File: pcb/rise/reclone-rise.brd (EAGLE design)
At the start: 85 x 56 mm, 11 parts, among them J1 MAGJACK, U1 6SLX25FTG256

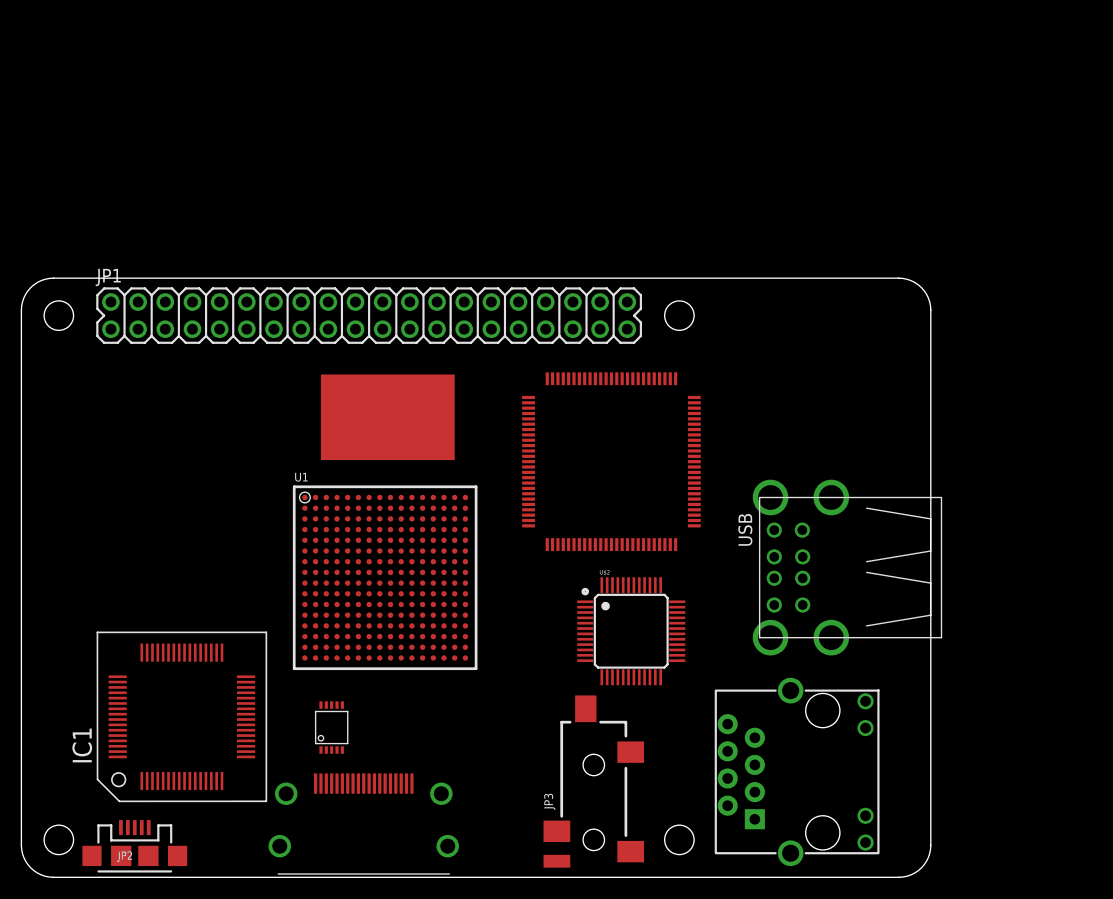
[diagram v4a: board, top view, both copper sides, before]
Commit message: Added Gadgeteer socket
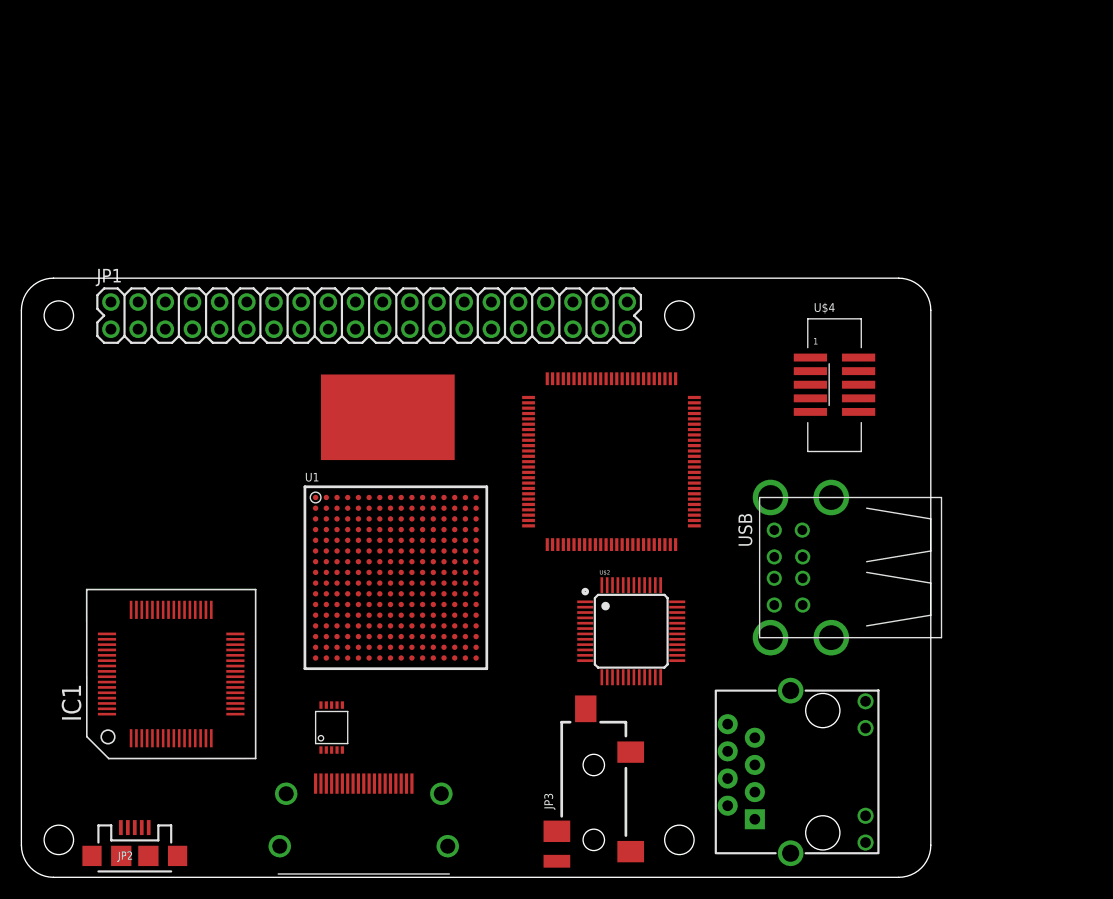
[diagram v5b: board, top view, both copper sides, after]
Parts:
- added U$4: SHF105, Gadgeteer:SHF105DSM_1
- U1: value 6SLX25FTG256 -> 6SLX16FTG256
- moved IC1 4.12 mm to (14.0, 19.0)
- moved U1 1.00 mm to (35.0, 28.0)
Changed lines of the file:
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@@
 <element name="USB" library="reclone-rise" package="USB-A-2H" value="USB_A_2H" x="69" y="29" locked="yes" rot="R180"/>
 <element name="MCU" library="reclone-rise" package="LQFP-100" value="STM32F407VGT6" x="48" y="46" rot="R270"/>
-<element name="U1" library="xilinx_devices_V6" package="FT256" value="6SLX25FTG256" x="34" y="28"/>
 <element name="JP1" library="SparkFun-Connectors" package="2X20" value="M20X2" x="32.5" y="52.5" locked="yes"/>
 <element name="J1" library="SparkFun-Connectors" package="MAGJACK" value="MAGJACK" x="86" y="2.25" locked="yes" rot="R90"/>
-<element name="IC1" library="ftdichip-3" package="TQFP64-12X12" value="" x="15" y="15"/>
+<element name="IC1" library="ftdichip-3" package="TQFP64-12X12" value="" x="14" y="19"/>
 <element name="JP2" library="SparkFun-Connectors" package="USB-MICROB" value="USB-MICROB" x="10.6" y="2" locked="yes">
 <attribute name="PROD_ID" value="CONN-09505" x="10.6" y="2" size="1.778" layer="27" display="off"/>
@@
 <element name="U$2" library="reclone-rise" package="LQFP-48" value="DP83848C" x="57" y="23"/>
 <element name="U$3" library="reclone-rise" package="HDMI_A_SMT" value="HDMI_A" x="32" y="4" locked="yes" rot="R270"/>
+<element name="U1" library="xilinx_devices_V6" package="FT256" value="6SLX16FTG256" x="35" y="28"/>
+<element name="U$4" library="Gadgeteer" package="SHF105DSM_1" value="SHF105" x="76" y="46"/>
 </elements>
 <signals>
 <signal name="GND">
+<contactref element="IC1" pad="1"/>
+<contactref element="IC1" pad="5"/>
+<contactref element="IC1" pad="11"/>
+<contactref element="IC1" pad="15"/>
+<contactref element="IC1" pad="25"/>
+<contactref element="IC1" pad="35"/>
+<contactref element="IC1" pad="47"/>
+<contactref element="IC1" pad="51"/>
 <contactref element="U1" pad="A1"/>
 <contactref element="U1" pad="A16"/>
@@
 <contactref element="U1" pad="T1"/>
 <contactref element="U1" pad="T16"/>
-<contactref element="IC1" pad="1"/>
-<contactref element="IC1" pad="5"/>
-<contactref element="IC1" pad="11"/>
-<contactref element="IC1" pad="15"/>
-<contactref element="IC1" pad="25"/>
-<contactref element="IC1" pad="35"/>
-<contactref element="IC1" pad="47"/>
-<contactref element="IC1" pad="51"/>
-<wire x1="38.5" y1="32.5" x2="41.5" y2="35.5" width="0" layer="19" extent="1-1"/>
-<wire x1="36.5" y1="34.5" x2="38.5" y2="32.5" width="0" layer="19" extent="1-1"/>
-<wire x1="40.5" y1="29.5" x2="38.5" y2="32.5" width="0" layer="19" extent="1-1"/>
-<wire x1="37.5" y1="28.5" x2="40.5" y2="29.5" width="0" layer="19" extent="1-1"/>
-<wire x1="34.5" y1="28.5" x2="37.5" y2="28.5" width="0" layer="19" extent="1-1"/>
-<wire x1="33.5" y1="29.5" x2="34.5" y2="28.5" width="0" layer="19" extent="1-1"/>
-<wire x1="32.5" y1="28.5" x2="33.5" y2="29.5" width="0" layer="19" extent="1-1"/>
-<wire x1="33.5" y1="27.5" x2="34.5" y2="28.5" width="0" layer="19" extent="1-1"/>
-<wire x1="34.5" y1="26.5" x2="33.5" y2="27.5" width="0" layer="19" extent="1-1"/>
-<wire x1="32.5" y1="26.5" x2="33.5" y2="27.5" width="0" layer="19" extent="1-1"/>
-<wire x1="34.5" y1="31.5" x2="33.5" y2="29.5" width="0" layer="19" extent="1-1"/>
-<wire x1="30.5" y1="27.5" x2="32.5" y2="28.5" width="0" layer="19" extent="1-1"/>
-<wire x1="33.5" y1="24.5" x2="34.5" y2="26.5" width="0" layer="19" extent="1-1"/>
-<wire x1="32.5" y1="34.5" x2="34.5" y2="31.5" width="0" layer="19" extent="1-1"/>
-<wire x1="29.5" y1="32.5" x2="32.5" y2="34.5" width="0" layer="19" extent="1-1"/>
-<wire x1="27.5" y1="29.5" x2="30.5" y2="27.5" width="0" layer="19" extent="1-1"/>
-<wire x1="35.5" y1="21.5" x2="33.5" y2="24.5" width="0" layer="19" extent="1-1"/>
-<wire x1="38.5" y1="23.5" x2="35.5" y2="21.5" width="0" layer="19" extent="1-1"/>
-<wire x1="40.5" y1="25.5" x2="38.5" y2="23.5" width="0" layer="19" extent="1-1"/>
-<wire x1="31.5" y1="21.5" x2="33.5" y2="24.5" width="0" layer="19" extent="1-1"/>
-<wire x1="28.5" y1="22.5" x2="31.5" y2="21.5" width="0" layer="19" extent="1-1"/>
-<wire x1="26.5" y1="20.5" x2="28.5" y2="22.5" width="0" layer="19" extent="1-1"/>
-<wire x1="27.5" y1="25.5" x2="28.5" y2="22.5" width="0" layer="19" extent="1-1"/>
-<wire x1="26.5" y1="35.5" x2="29.5" y2="32.5" width="0" layer="19" extent="1-1"/>
-<wire x1="41.5" y1="20.5" x2="38.5" y2="23.5" width="0" layer="19" extent="1-1"/>
-<wire x1="11.7499" y1="21.0001" x2="26.5" y2="20.5" width="0" layer="19" extent="1-1"/>
-<wire x1="8.9999" y1="17.75" x2="11.7499" y2="21.0001" width="0" layer="19" extent="1-1"/>
-<wire x1="17.7501" y1="21.0001" x2="11.7499" y2="21.0001" width="0" layer="19" extent="1-1"/>
-<wire x1="21.0001" y1="15.25" x2="17.7501" y2="21.0001" width="0" layer="19" extent="1-1"/>
-<wire x1="18.25" y1="8.9999" x2="21.0001" y2="15.25" width="0" layer="19" extent="1-1"/>
-<wire x1="16.25" y1="8.9999" x2="18.25" y2="8.9999" width="0" layer="19" extent="1-1"/>
-<wire x1="13.25" y1="8.9999" x2="16.25" y2="8.9999" width="0" layer="19" extent="1-1"/>
-<wire x1="11.25" y1="8.9999" x2="13.25" y2="8.9999" width="0" layer="19" extent="1-1"/>
+<wire x1="16.7501" y1="25.0001" x2="20.0001" y2="19.25" width="0" layer="19" extent="1-1"/>
+<wire x1="10.7499" y1="25.0001" x2="16.7501" y2="25.0001" width="0" layer="19" extent="1-1"/>
+<wire x1="7.9999" y1="21.75" x2="10.7499" y2="25.0001" width="0" layer="19" extent="1-1"/>
+<wire x1="17.25" y1="12.9999" x2="20.0001" y2="19.25" width="0" layer="19" extent="1-1"/>
+<wire x1="15.25" y1="12.9999" x2="17.25" y2="12.9999" width="0" layer="19" extent="1-1"/>
+<wire x1="12.25" y1="12.9999" x2="15.25" y2="12.9999" width="0" layer="19" extent="1-1"/>
+<wire x1="10.25" y1="12.9999" x2="12.25" y2="12.9999" width="0" layer="19" extent="1-1"/>
+<wire x1="42.5" y1="35.5" x2="7.9999" y2="21.75" width="0" layer="19" extent="1-1"/>
+<wire x1="39.5" y1="32.5" x2="42.5" y2="35.5" width="0" layer="19" extent="1-1"/>
+<wire x1="37.5" y1="34.5" x2="39.5" y2="32.5" width="0" layer="19" extent="1-1"/>
+<wire x1="41.5" y1="29.5" x2="39.5" y2="32.5" width="0" layer="19" extent="1-1"/>
+<wire x1="38.5" y1="28.5" x2="41.5" y2="29.5" width="0" layer="19" extent="1-1"/>
+<wire x1="35.5" y1="28.5" x2="38.5" y2="28.5" width="0" layer="19" extent="1-1"/>
+<wire x1="34.5" y1="27.5" x2="35.5" y2="28.5" width="0" layer="19" extent="1-1"/>
+<wire x1="33.5" y1="28.5" x2="34.5" y2="27.5" width="0" layer="19" extent="1-1"/>
+<wire x1="33.5" y1="26.5" x2="34.5" y2="27.5" width="0" layer="19" extent="1-1"/>
+<wire x1="35.5" y1="26.5" x2="34.5" y2="27.5" width="0" layer="19" extent="1-1"/>
+<wire x1="34.5" y1="29.5" x2="35.5" y2="28.5" width="0" layer="19" extent="1-1"/>
+<wire x1="31.5" y1="27.5" x2="33.5" y2="28.5" width="0" layer="19" extent="1-1"/>
+<wire x1="34.5" y1="24.5" x2="33.5" y2="26.5" width="0" layer="19" extent="1-1"/>
+<wire x1="35.5" y1="31.5" x2="34.5" y2="29.5" width="0" layer="19" extent="1-1"/>
+<wire x1="28.5" y1="25.5" x2="31.5" y2="27.5" width="0" layer="19" extent="1-1"/>
+<wire x1="29.5" y1="22.5" x2="28.5" y2="25.5" width="0" layer="19" extent="1-1"/>
+<wire x1="27.5" y1="20.5" x2="29.5" y2="22.5" width="0" layer="19" extent="1-1"/>
+<wire x1="32.5" y1="21.5" x2="29.5" y2="22.5" width="0" layer="19" extent="1-1"/>
+<wire x1="28.5" y1="29.5" x2="31.5" y2="27.5" width="0" layer="19" extent="1-1"/>
+<wire x1="36.5" y1="21.5" x2="34.5" y2="24.5" width="0" layer="19" extent="1-1"/>
+<wire x1="33.5" y1="34.5" x2="35.5" y2="31.5" width="0" layer="19" extent="1-1"/>
+<wire x1="30.5" y1="32.5" x2="28.5" y2="29.5" width="0" layer="19" extent="1-1"/>
+<wire x1="39.5" y1="23.5" x2="36.5" y2="21.5" width="0" layer="19" extent="1-1"/>
+<wire x1="41.5" y1="25.5" x2="39.5" y2="23.5" width="0" layer="19" extent="1-1"/>
+<wire x1="27.5" y1="35.5" x2="30.5" y2="32.5" width="0" layer="19" extent="1-1"/>
+<wire x1="42.5" y1="20.5" x2="39.5" y2="23.5" width="0" layer="19" extent="1-1"/>
 </signal>
 <signal name="AGND">
@@
 <contactref element="IC1" pad="37"/>
 <contactref element="IC1" pad="64"/>
-<wire x1="16.7499" y1="8.9999" x2="16.7501" y2="21.0001" width="0" layer="19" extent="1-1"/>
-<wire x1="8.9999" y1="11.2499" x2="16.7499" y2="8.9999" width="0" layer="19" extent="1-1"/>
+<wire x1="15.7499" y1="12.9999" x2="15.7501" y2="25.0001" width="0" layer="19" extent="1-1"/>
+<wire x1="7.9999" y1="15.2499" x2="15.7499" y2="12.9999" width="0" layer="19" extent="1-1"/>
 </signal>
 <signal name="VCCIO">
@@
 <contactref element="IC1" pad="42"/>
 <contactref element="IC1" pad="56"/>
-<wire x1="21.0001" y1="12.7501" x2="21.0001" y2="18.2469" width="0" layer="19" extent="1-1"/>
-<wire x1="14.25" y1="21.0001" x2="21.0001" y2="18.2469" width="0" layer="19" extent="1-1"/>
-<wire x1="8.9999" y1="15.2501" x2="14.25" y2="21.0001" width="0" layer="19" extent="1-1"/>
+<wire x1="20.0001" y1="16.7501" x2="20.0001" y2="22.2469" width="0" layer="19" extent="1-1"/>
+<wire x1="13.25" y1="25.0001" x2="20.0001" y2="22.2469" width="0" layer="19" extent="1-1"/>
+<wire x1="7.9999" y1="19.2501" x2="13.25" y2="25.0001" width="0" layer="19" extent="1-1"/>
 </signal>
 <signal name="VPLL">

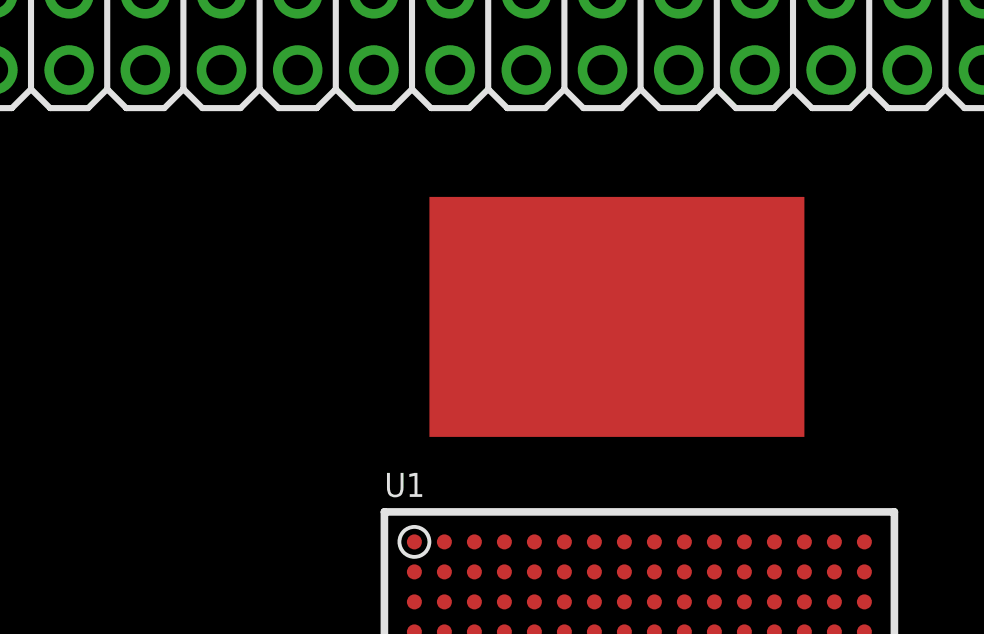
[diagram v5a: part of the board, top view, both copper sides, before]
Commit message: Finished a basic DDR2 SDRAM part
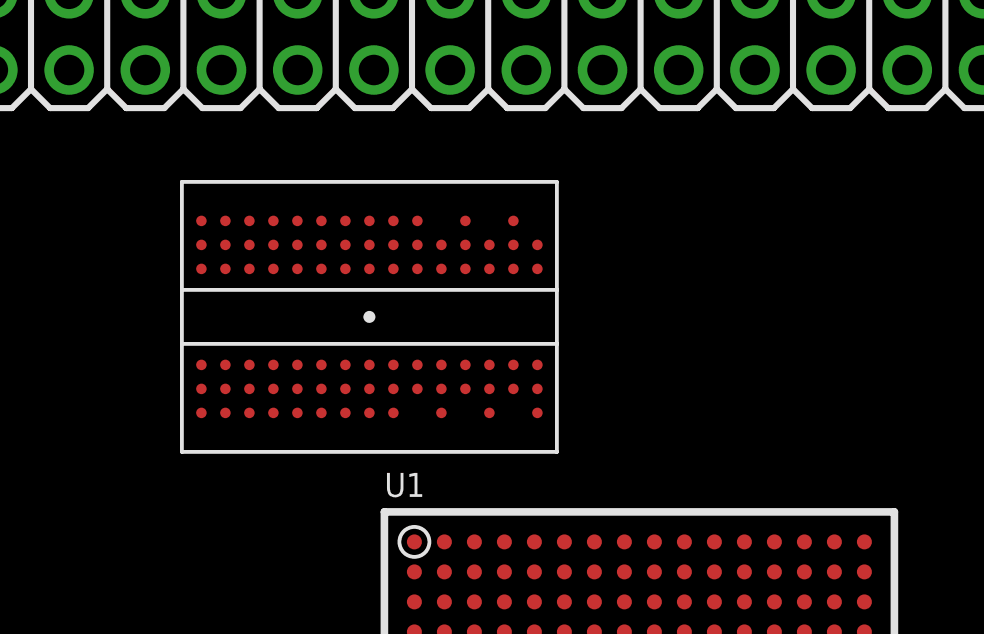
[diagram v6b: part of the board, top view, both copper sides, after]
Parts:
- added U$5: MT47H128M16, reclone-rise:84-FBGA-9X12.5
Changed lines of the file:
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@@
 <hole x="61.5" y="52.5" drill="2.75"/>
 <hole x="61.5" y="3.5" drill="2.75"/>
-<rectangle x1="28" y1="39" x2="40.5" y2="47" layer="1"/>
 </plain>
 <attributes>
@@
 <element name="U1" library="xilinx_devices_V6" package="FT256" value="6SLX16FTG256" x="35" y="28"/>
 <element name="U$4" library="Gadgeteer" package="SHF105DSM_1" value="SHF105" x="76" y="46"/>
+<element name="U$5" library="reclone-rise" package="84-FBGA-9X12.5" value="MT47H128M16" x="26" y="43" rot="R90"/>
 </elements>
 <signals>
